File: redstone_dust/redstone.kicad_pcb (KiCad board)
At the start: 2 copper layers, 40 x 40 mm, 76 parts, among them J1 1x4_Pogo, J2 1x4_Pogo, J3 1x4_Pogo, J4 1x4_Pogo, J5 1x4_Pogo, J6 1x4_Pogo, J7 1x4_Pogo, J8 1x4_Pogo, J9 2.54mm_ProgrammingPin, Q1 MMBT3904, Q2 MMBT3904, Q3 MMBT3904, Q4 MMBT3904, SW1 SW_Push_Open, U1 RP2040, U2 RBT05W24S05, U3 TPS62162DSG, U5 W25Q16JVSS

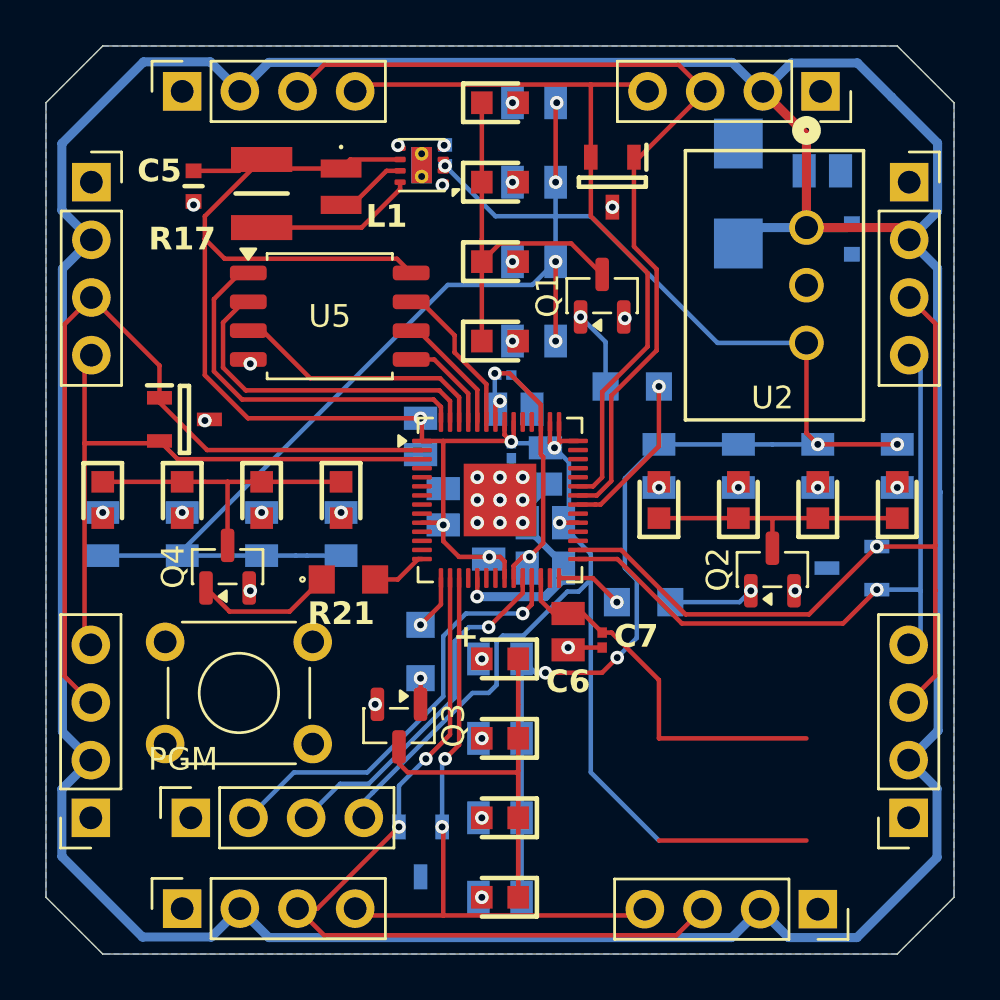
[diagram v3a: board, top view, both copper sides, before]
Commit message: move reset buttom and add dip switch
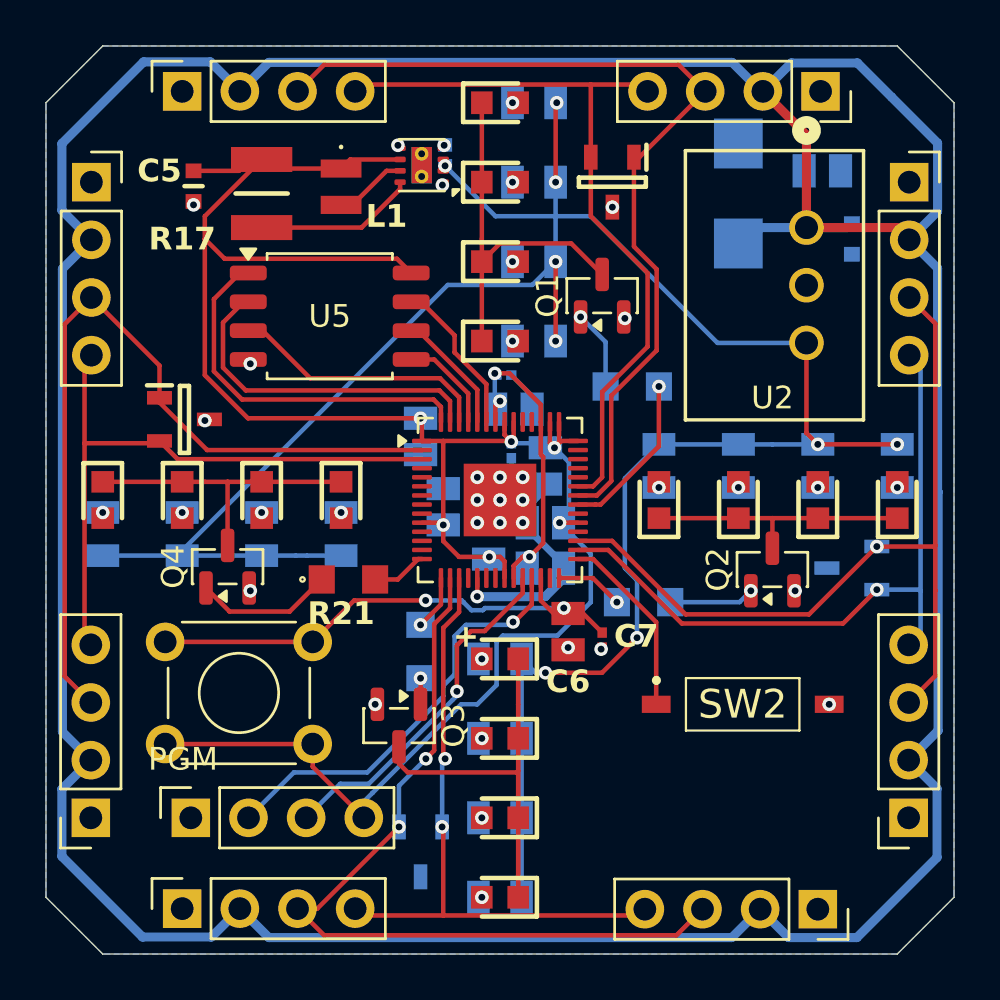
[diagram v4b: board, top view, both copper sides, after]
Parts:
- added SW2: SW_DIP_x01, SamacSys_Parts:416131160801, F.Cu at (145.7, 64.0)
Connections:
- U1 pad 29: /E_RX -> Net-(U1-GPIO18)
- U1 pad 30: /E_TX -> /E_RX
- U1 pad 31: unconnected-(U1-GPIO20-Pad31) -> /E_TX
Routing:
- net Net-(U1-GPIO18): track 0.00 -> 8.21 mm
- net /3.3V_LOCAL: track 104.2 -> 96.2 mm
- net Net-(SW1-B): track 16.7 -> 23.1 mm, vias 0 -> 2
- net GND: track 16.7 -> 15.4 mm, vias 22 -> 24

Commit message: add four individually controlled leds for repeater, small adjustments for redstone dust
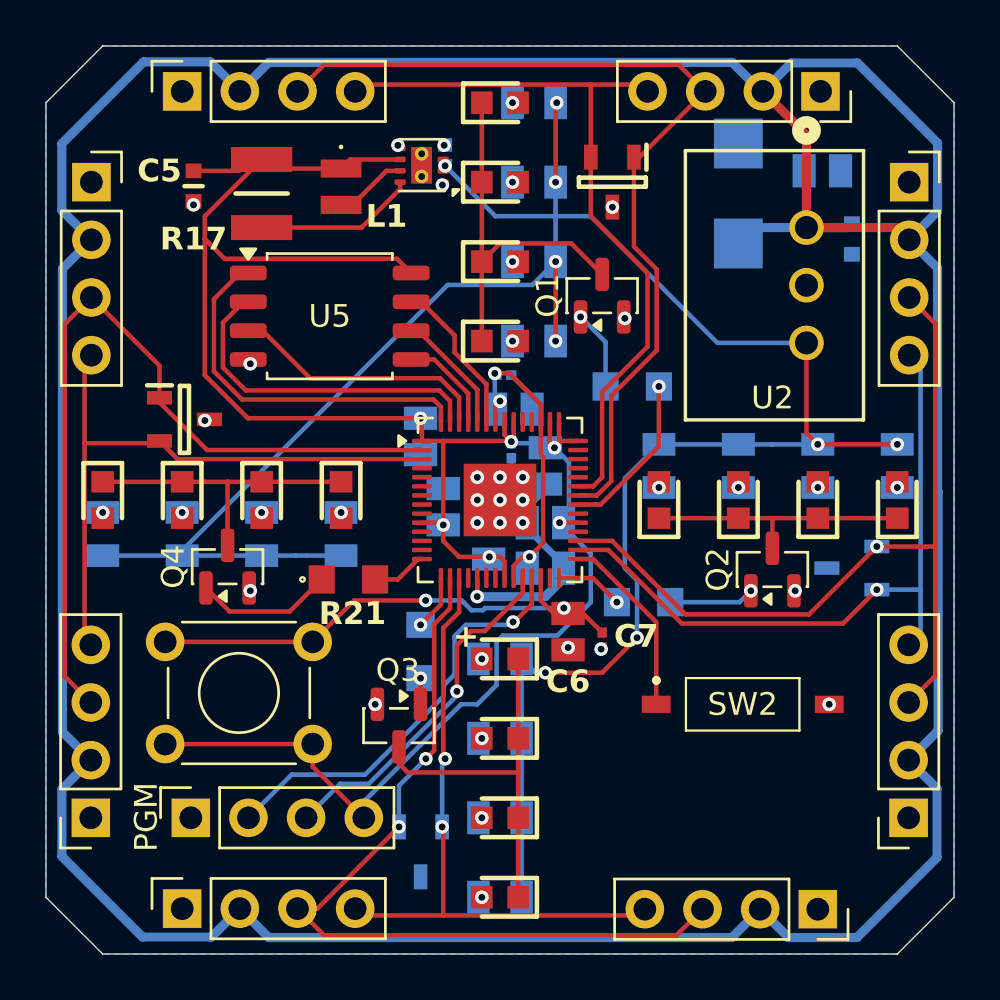
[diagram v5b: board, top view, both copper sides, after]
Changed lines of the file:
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@@
 		(tags "SOT TO_SOT_SMD")
 		(property "Reference" "Q3"
-			(at 0 -2.4 90)
+			(at -2.4375 0.05 180)
 			(layer "F.SilkS")
 			(effects
@@
 		(tags "Resistor")
 		(property "Reference" "R21"
-			(at -0.325 1.5 0)
+			(at 0.175 1.5 0)
 			(layer "F.SilkS")
 			(effects
@@
 		(tags "Resistor")
 		(property "Reference" "R17"
-			(at 2 3.5 180)
+			(at 2 3 180)
 			(layer "F.SilkS")
 			(effects
@@
 			(effects
 				(font
-					(size 1.27 1.27)
-					(thickness 0.254)
+					(size 1 1)
+					(thickness 0.15)
 				)
 			)
@@
 		(tags "Capacitor")
 		(property "Reference" "C10"
-			(at 2.89 0 0)
+			(at 2.39 -0.5 90)
 			(layer "B.SilkS")
 			(effects
@@
 		(tags "Resistor")
 		(property "Reference" "R18"
-			(at 0 1.5 0)
+			(at 0.175 -1.5 0)
 			(layer "B.SilkS")
 			(effects
@@
 	)
 	(gr_text "PGM"
-		(at 119.5 67 0)
+		(at 120 70.5 90)
 		(layer "F.SilkS")
 		(effects
@@
 	)
 	(segment
-		(start 141.5 45)
-		(end 141.5 48.244206)
-		(width 0.2)
-		(layer "F.Cu")
-		(net 26)
-	)
-	(segment
 		(start 141.5 48.244206)
 		(end 139.5 50.244206)
@@
 	(segment
 		(start 139 39.9)
-		(end 139 42.5)
+		(end 139 36.699)
 		(width 0.2)
 		(layer "F.Cu")
@@
 	)
 	(segment
-		(start 139 39.9)
-		(end 139 36.699)
+		(start 139.5 54)
+		(end 139.100001 54.399999)
 		(width 0.2)
 		(layer "F.Cu")
@@
 	)
 	(segment
-		(start 139 42.5)
-		(end 141.5 45)
+		(start 139.100001 54.399999)
+		(end 138.4375 54.399999)
 		(width 0.2)
 		(layer "F.Cu")
@@
 	)
 	(segment
+		(start 141.5 45)
+		(end 141.5 48.244206)
+		(width 0.2)
+		(layer "F.Cu")
+		(net 26)
+	)
+	(segment
 		(start 139 36.699)
 		(end 128.921 36.699)
@@
 	)
 	(segment
-		(start 139.5 54)
-		(end 139.100001 54.399999)
+		(start 139 39.9)
+		(end 139 42.5)
 		(width 0.2)
 		(layer "F.Cu")
@@
 	)
 	(segment
-		(start 139.100001 54.399999)
-		(end 138.4375 54.399999)
+		(start 139 36.699)
+		(end 141.199 36.699)
 		(width 0.2)
 		(layer "F.Cu")
@@
 	)
 	(segment
-		(start 139 36.699)
-		(end 141.199 36.699)
+		(start 139 42.5)
+		(end 141.5 45)
 		(width 0.2)
 		(layer "F.Cu")
@@
 	)
 	(segment
-		(start 132.502 60.6322)
-		(end 133.2 59.9342)
-		(width 0.2)
-		(layer "F.Cu")
-		(net 30)
-	)
-	(segment
-		(start 132.583255 66.4)
-		(end 132.502 66.318745)
-		(width 0.2)
-		(layer "F.Cu")
-		(net 30)
-	)
-	(segment
 		(start 128.921 73.301)
 		(end 128.62 73)
@@
 	)
 	(segment
-		(start 133.2 59.9342)
-		(end 133.2 58.4375)
+		(start 132.502 66.318745)
+		(end 132.502 60.6322)
 		(width 0.2)
 		(layer "F.Cu")
@@
 	)
 	(segment
-		(start 132.502 66.318745)
-		(end 132.502 60.6322)
+		(start 132.502 60.6322)
+		(end 133.2 59.9342)
+		(width 0.2)
+		(layer "F.Cu")
+		(net 30)
+	)
+	(segment
+		(start 133.2 59.9342)
+		(end 133.2 58.4375)
+		(width 0.2)
+		(layer "F.Cu")
+		(net 30)
+	)
+	(segment
+		(start 132.583255 66.4)
+		(end 132.502 66.318745)
 		(width 0.2)
 		(layer "F.Cu")
@@
 	)
 	(segment
-		(start 132.45 66.533255)
-		(end 132.45 69.4)
+		(start 132.583255 66.4)
+		(end 132.45 66.533255)
 		(width 0.2)
 		(layer "B.Cu")
@@
 	)
 	(segment
-		(start 132.583255 66.4)
-		(end 132.45 66.533255)
+		(start 132.45 66.533255)
+		(end 132.45 69.4)
 		(width 0.2)
 		(layer "B.Cu")
@@
 	)
 	(segment
-		(start 132.501 63.180031)
-		(end 132.501 63.651)
+		(start 133 62.681031)
+		(end 132.501 63.180031)
 		(width 0.2)
 		(layer "B.Cu")
@@
 	)
 	(segment
-		(start 132.501 63.651)
-		(end 129.152 67)
+		(start 125.821 67.099)
+		(end 123.92 69)
 		(width 0.2)
 		(layer "B.Cu")
@@
 	)
 	(segment
-		(start 129.152 67)
-		(end 125.92 67)
+		(start 132.501 63.651)
+		(end 129.053 67.099)
 		(width 0.2)
 		(layer "B.Cu")
@@
 	)
 	(segment
-		(start 133 62.681031)
-		(end 132.501 63.180031)
+		(start 132.501 63.180031)
+		(end 132.501 63.651)
 		(width 0.2)
 		(layer "B.Cu")
@@
 	)
 	(segment
-		(start 133 61)
-		(end 133 62.681031)
+		(start 129.053 67.099)
+		(end 125.821 67.099)
 		(width 0.2)
 		(layer "B.Cu")
@@
 	)
 	(segment
-		(start 125.92 67)
-		(end 123.92 69)
+		(start 133 61)
+		(end 133 62.681031)
 		(width 0.2)
 		(layer "B.Cu")
